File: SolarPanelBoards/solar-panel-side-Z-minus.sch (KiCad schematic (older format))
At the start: 25 parts, among them J1 Conn_01x06, J2 SMA Connector Male, U1 OPT3001DNPT, U2 HHM1589D1

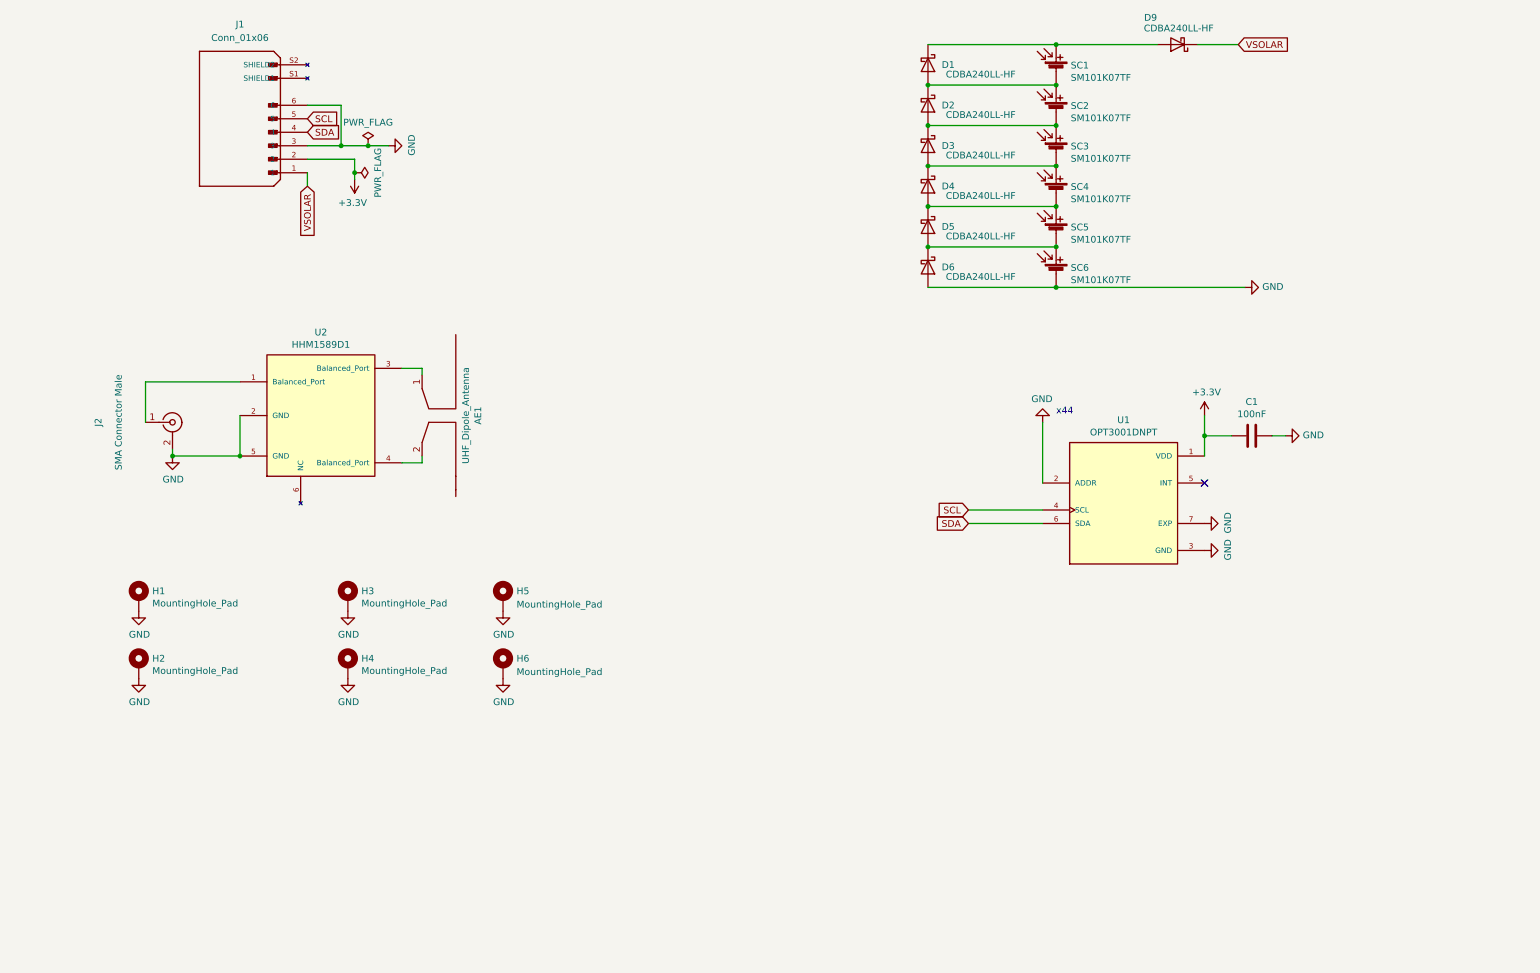
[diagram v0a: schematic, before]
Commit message: Battery board and side panels ready for CAD check and review, pycubed not finished yet
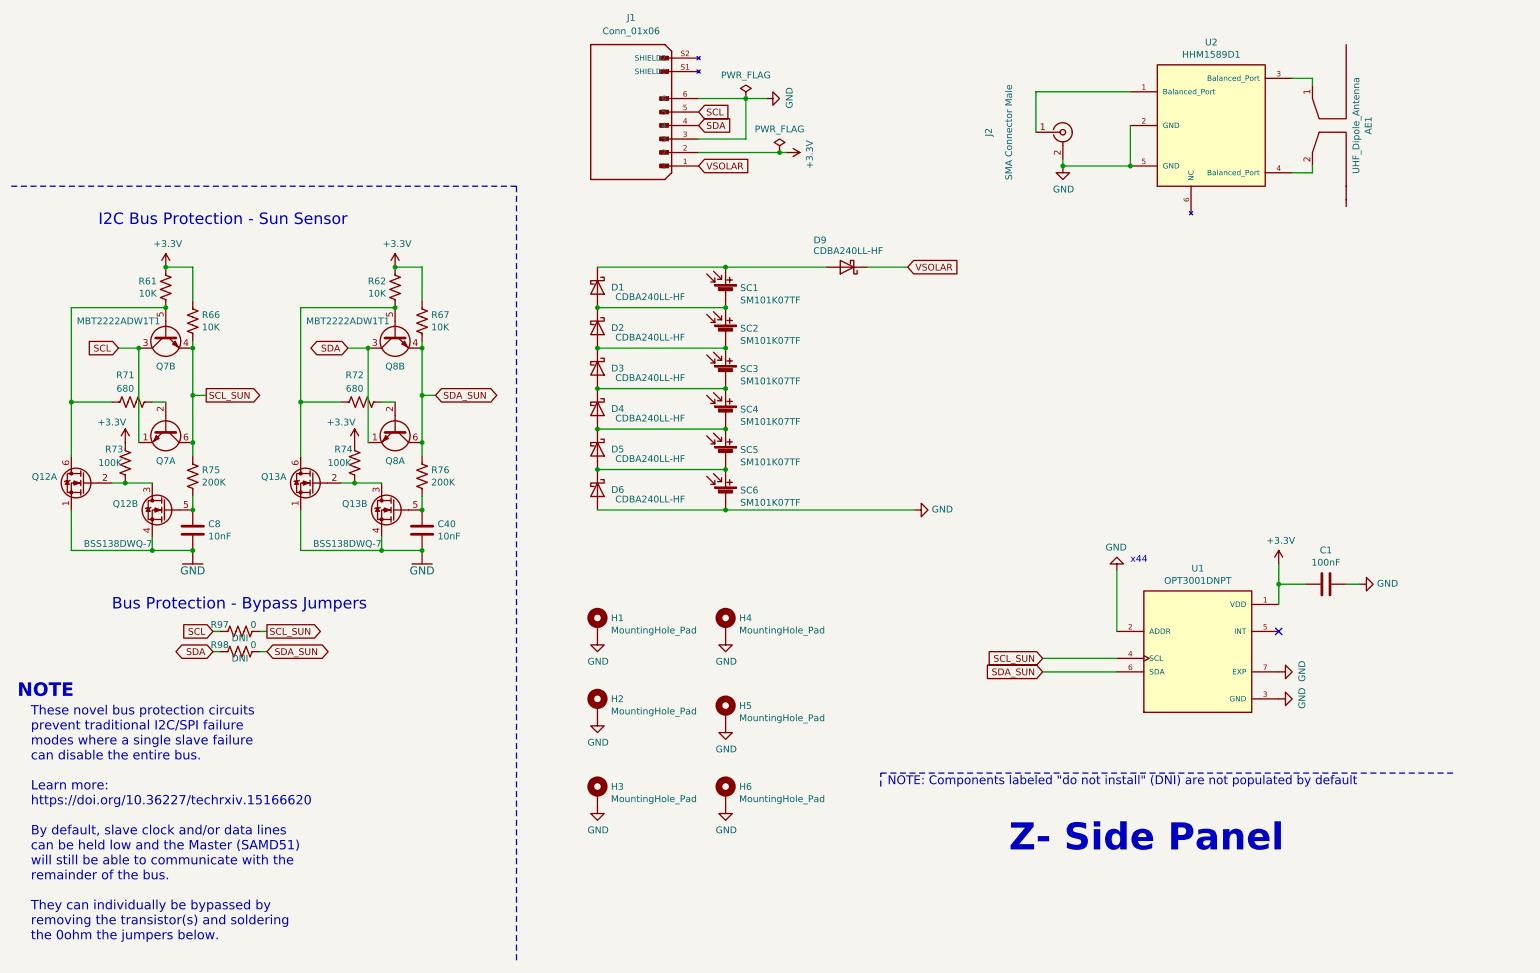
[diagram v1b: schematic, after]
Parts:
- added C40, C8: 10nF, Capacitor_SMD:C_0603_1608Metric, symbol Device:C
- added Q12, Q13: BSS138DWQ-7, sapling:BSS138DWQ-7, symbol mainboard:BSS138DWQ-7
- added Q7, Q8: MBT2222ADW1T1, Package_TO_SOT_SMD:SOT-363_SC-70-6, symbol Transistor_BJT:MBT2222ADW1T1
- added R61, R62, R66, R67: 10K, Resistor_SMD:R_0603_1608Metric, symbol Device:R_US
- added R71, R72: 680, Resistor_SMD:R_0603_1608Metric, symbol Device:R_US
- added R73, R74: 100K, Resistor_SMD:R_0603_1608Metric, symbol Device:R_US
- added R75, R76: 200K, Resistor_SMD:R_0603_1608Metric, symbol Device:R_US
- added R97, R98: 0, Resistor_SMD:R_0603_1608Metric, symbol Device:R_US
- H1, H2: footprint MountingHole:MountingHole_3.2mm_M3_DIN965_Pad_TopBottom -> MountingHole:MountingHole_2.2mm_M2_DIN965_Pad_TopBottom
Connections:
- net +3V3: now also R61.1, R62.1, R66.1, R67.1, R73.1, R74.1
- net SCL: now also Q7.1 (E1), Q7.3 (C2), R97.2; no longer U1.4 (SCL)
- net SDA: now also Q8.1 (E1), Q8.3 (C2), R98.2; no longer U1.6 (SDA)
- new net: C8.2, Q12.1 (S2), Q12.4 (S1)
- new net: Q12.2 (G2), Q12.3 (D2), R73.2
- new net: Q12.6 (D1), Q7.5 (B2), R61.2, R71.2
- new net: C8.1, Q12.5 (G1), R75.2
- new net: Q7.2 (B1), R71.1
- new net: Q8.2 (B1), R72.1
- new net: Q13.6 (D1), Q8.5 (B2), R62.2, R72.2
- new net: C40.1, Q13.5 (G1), R76.2
- new net: C40.2, Q13.1 (S2), Q13.4 (S1)
- new net: Q13.2 (G2), Q13.3 (D2), R74.2
- new net SCL_SUN: Q7.4 (E2), Q7.6 (C1), R66.2, R75.1, R97.1, U1.4 (SCL)
- new net SDA_SUN: Q8.4 (E2), Q8.6 (C1), R67.2, R76.1, R98.1, U1.6 (SDA)
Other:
- note added: "Bus Protection - Bypass Jumpers"
- note added: "I2C Bus Protection - Sun Sensor"
- note added: "NOTE"
- note added: "NOTE: Components labeled "do not install" (DNI) are not populated by default"
- note added: "These novel bus protection circuits\nprevent traditional I2C/SPI failure \nmodes where a single slave failure\ncan disable the entire bus.\n\nLearn more: \nhttps://doi.org/10.36227/techrxiv.15166620\n\nBy default, slave clock and/or data lines \ncan be held low and the Master (SAMD51) \nwill still be able to communicate with the \nremainder of the bus.\n\nThey can individually be bypassed by \nre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"
- note added: "Z- Side Panel"
- moved on the sheet: AE1, D2, D5, D6, J2, SC2, SC5, SC6, U2

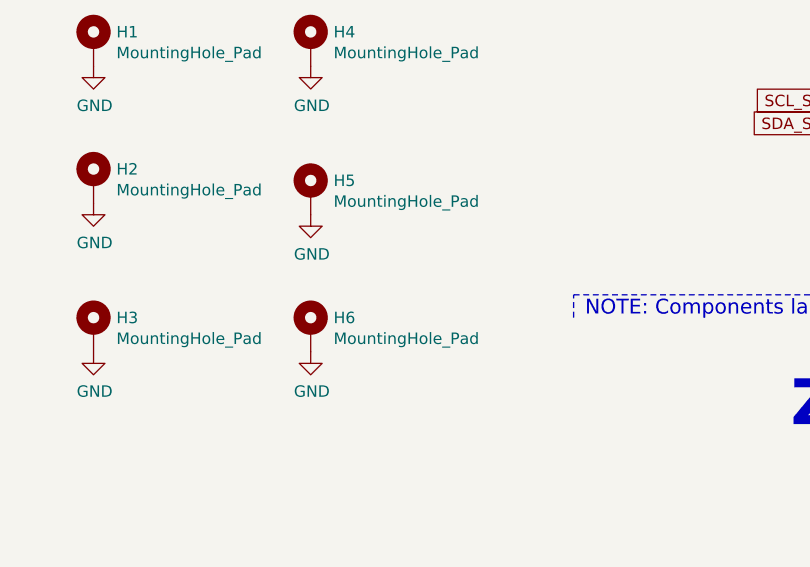
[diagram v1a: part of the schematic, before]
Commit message: Z- finished, new radio traces and edges
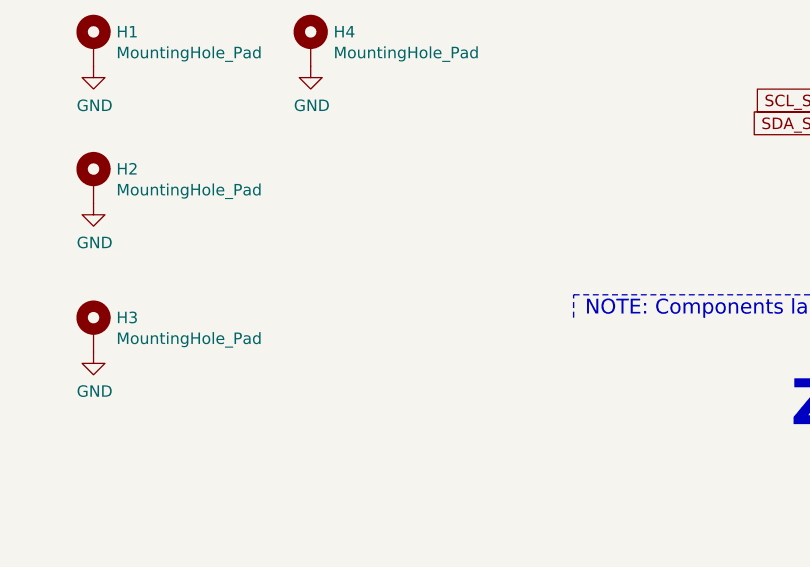
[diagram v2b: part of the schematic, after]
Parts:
- removed H5, H6: MountingHole_Pad, MountingHole:MountingHole_2.2mm_M2_DIN965_Pad_TopBottom, symbol Mechanical:MountingHole_Pad
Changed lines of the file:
@@
-$EndComp
-$Comp
-L Mechanical:MountingHole_Pad H5
-U 1 1 618807A3
-P 5800 5950
-F 0 "H5" H 5900 5999 50  0000 L CNN
-F 1 "MountingHole_Pad" H 5900 5908 50  0000 L CNN
-F 2 "MountingHole:MountingHole_2.2mm_M2_DIN965_Pad_TopBottom" H 5800 5950 50  0001 C CNN
-F 3 "~" H 5800 5950 50  0001 C CNN
-	1    5800 5950
-	1    0    0    -1
-$EndComp
-$Comp
-L power:GND #PWR05
-U 1 1 618807A9
-P 5800 6050
-F 0 "#PWR05" H 5800 5800 50  0001 C CNN
-F 1 "GND" H 5805 5877 50  0000 C CNN
-F 2 "" H 5800 6050 50  0001 C CNN
-F 3 "" H 5800 6050 50  0001 C CNN
-	1    5800 6050
-	1    0    0    -1
 $EndComp
 $Comp
@@
 	1    0    0    -1
 $EndComp
-$Comp
-L Mechanical:MountingHole_Pad H6
-U 1 1 6188213B
-P 5800 6550
-F 0 "H6" H 5900 6599 50  0000 L CNN
-F 1 "MountingHole_Pad" H 5900 6508 50  0000 L CNN
-F 2 "MountingHole:MountingHole_2.2mm_M2_DIN965_Pad_TopBottom" H 5800 6550 50  0001 C CNN
-F 3 "~" H 5800 6550 50  0001 C CNN
-	1    5800 6550
-	1    0    0    -1
-$EndComp
-$Comp
-L power:GND #PWR06
-U 1 1 61882141
-P 5800 6650
-F 0 "#PWR06" H 5800 6400 50  0001 C CNN
-F 1 "GND" H 5805 6477 50  0000 C CNN
-F 2 "" H 5800 6650 50  0001 C CNN
-F 3 "" H 5800 6650 50  0001 C CNN
-	1    5800 6650
-	1    0    0    -1
-$EndComp
